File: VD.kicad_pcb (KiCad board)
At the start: 4 copper layers, 95 x 60 mm, 148 parts, among them J1 TC2030 NL, J10 Screw_Terminal_01x02, J11 Screw_Terminal_01x08, J12 Screw_Terminal_01x08, J13 Screw_Terminal_01x08, J2 USB_C_Receptacle_USB2.0_16P, J3 Conn_02x06_Top_Bottom, J4 Screw_Terminal_01x02, J5 Conn_02x01, J6 Conn_02x01, J7 Screw_Terminal_01x05, J8 RJ45_Hanrun_HR911105A_Horizon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, J9 Screw_Terminal_01x02, SW1 SKRPANE010, U1 USBLC6-2SC6, U10 IPS4140HQ, U11 PS2841-4B, U12 PS2841-4B, U13 IPS4140HQ, U14 PS2841-4B, U15 PS2841-4B, U2 STM32H563RIVx, U3 AP2112K-3.3, U4 TCAN1462V, U5 LAN8742A, U6 PC817, U7 IPS4140HQ, U8 PS2841-4B, U9 PS2841-4B, Y1 25 MHz, Y2 25 MHz

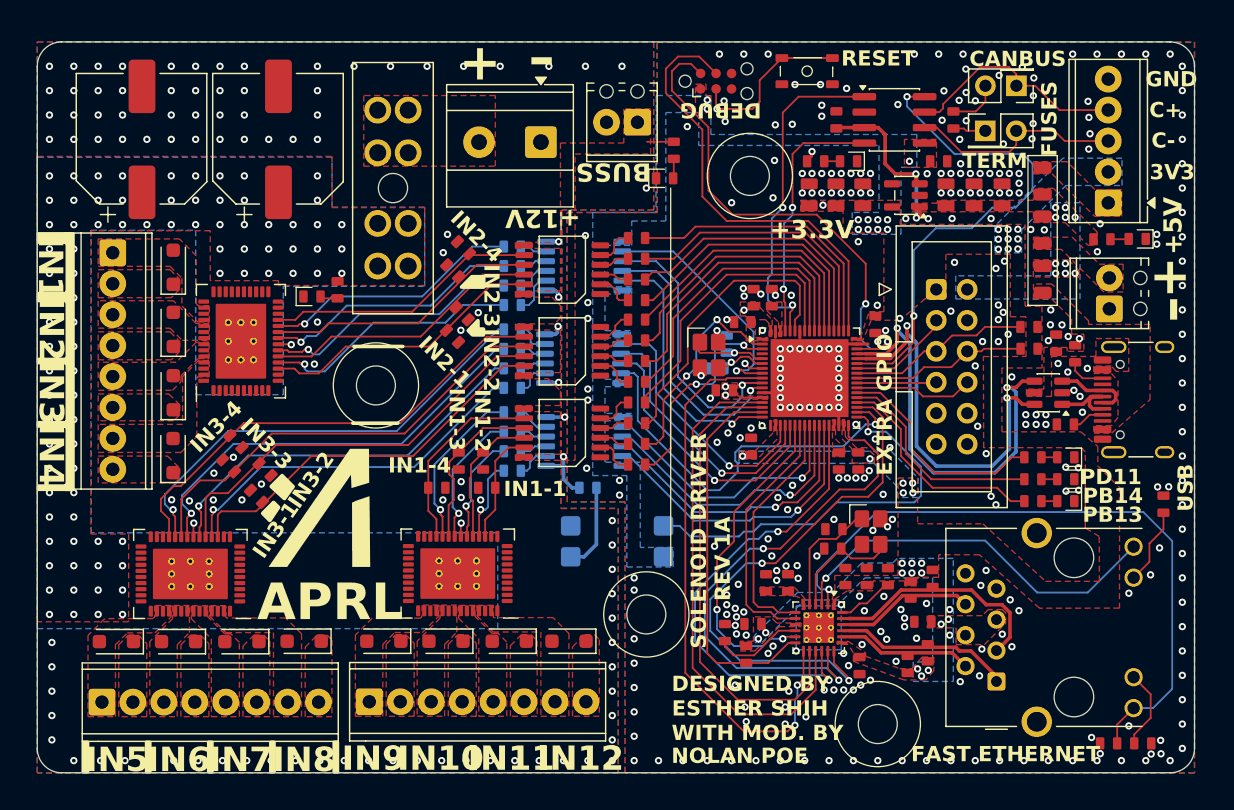
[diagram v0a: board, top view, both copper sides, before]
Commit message: Update silkscreens and nets
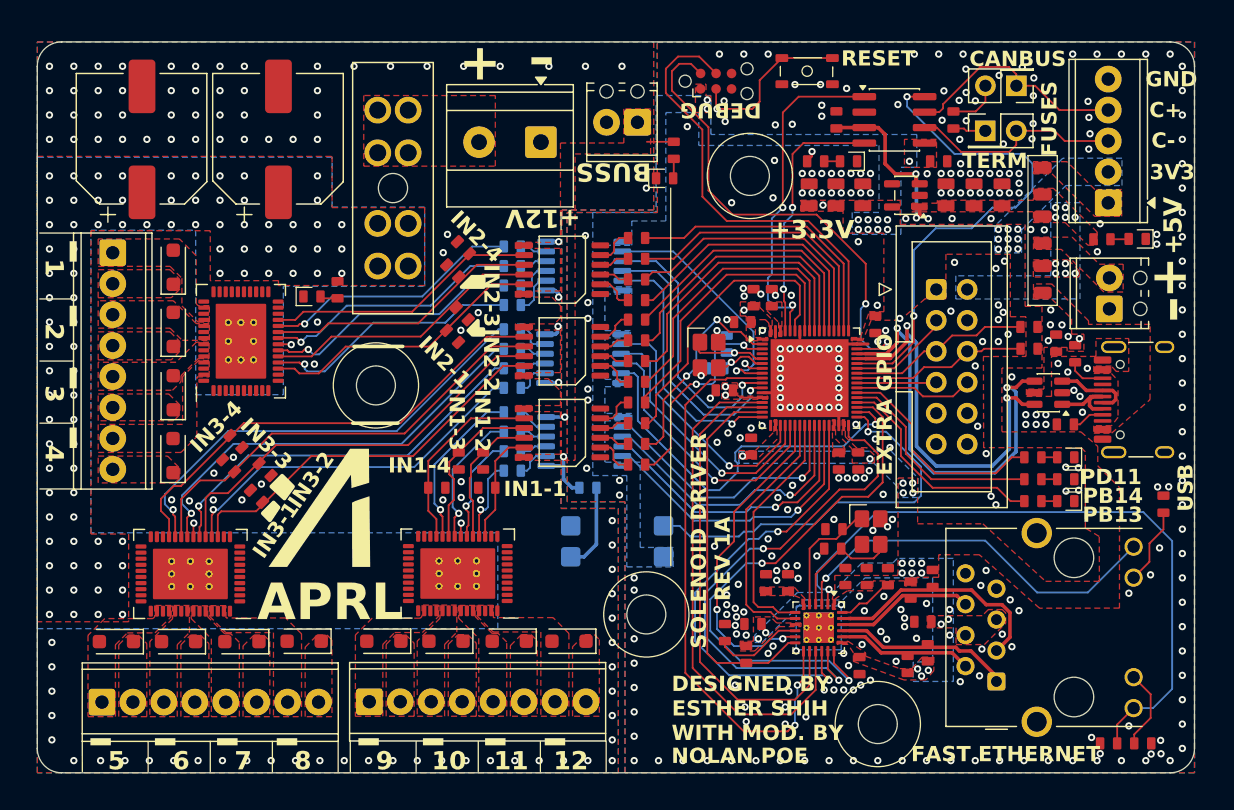
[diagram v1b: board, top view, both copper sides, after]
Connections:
- net +24V renamed +12V
- net +24V_SAFE renamed +12V_SAFE
- net /Power/+24_IN renamed /Power/+12_IN
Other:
- board text added: "1"
- board text added: "10"
- board text added: "11"
- board text added: "12"
- board text added: "2"
- board text added: "3"
- board text added: "4"
- board text added: "5"
- board text added: "6"
- board text added: "7"
- board text added: "8"
- board text added: "9"
- board text removed: "IN1"
- board text removed: "IN10"
- board text removed: "IN11"
- board text removed: "IN12"
- board text removed: "IN2"
- board text removed: "IN3"
- board text removed: "IN4"
- board text removed: "IN5"
- board text removed: "IN6"
- board text removed: "IN7"
- board text removed: "IN8"
- board text removed: "IN9"

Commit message: Small stuff
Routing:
- net GNDPWR: vias 106 -> 131
- net GND: vias 328 -> 329
